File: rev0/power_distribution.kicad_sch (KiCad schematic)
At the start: 84 parts, among them Q1 PMOS, Q10 2PNP, Q11 2NPN, Q12 PMOS, Q13 2PNP, Q14 2PNP, Q15 2PNP, Q2 PMOS, Q3 2NPN, Q4 PMOS, Q5 PMOS, Q6 PMOS, Q7 PMOS, Q8 2NPN, Q9 PMOS, U1 PAC1954

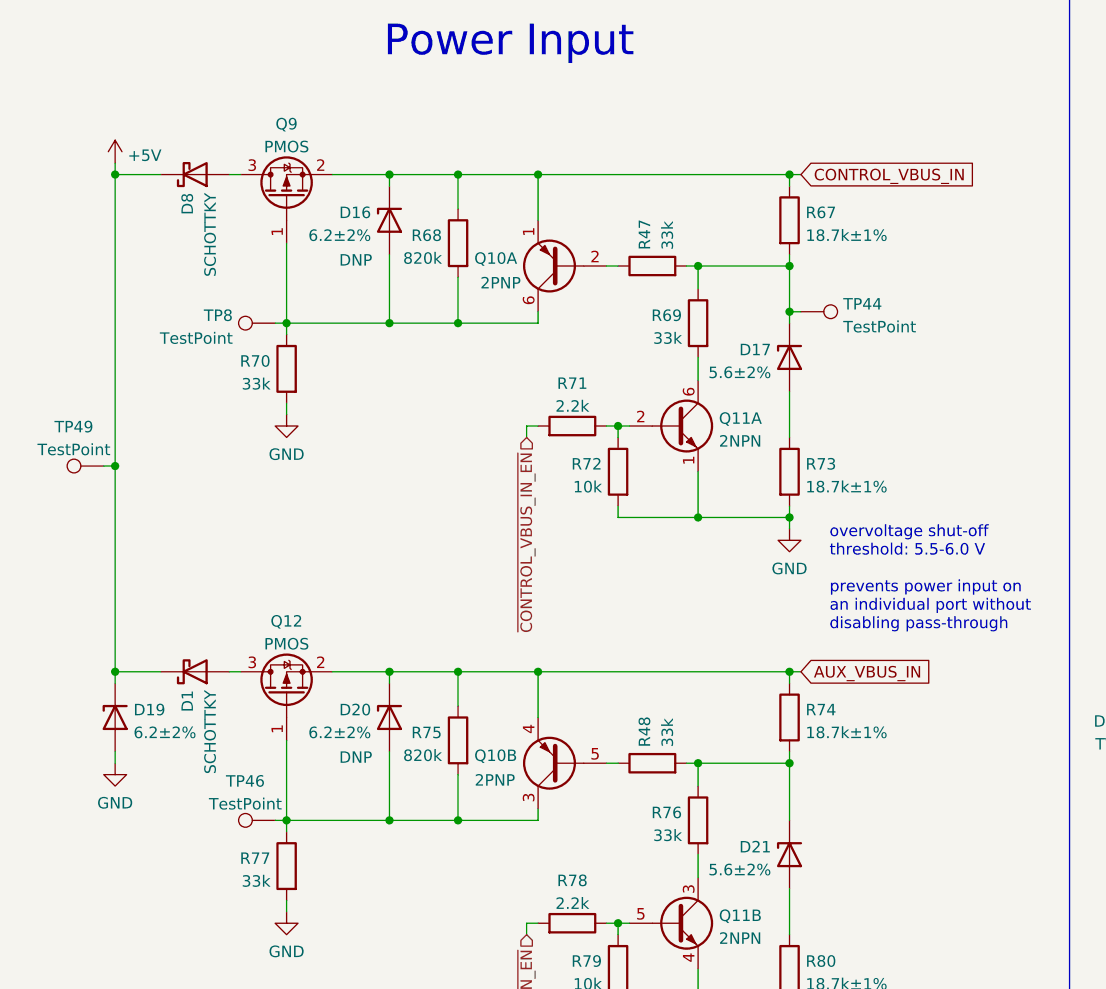
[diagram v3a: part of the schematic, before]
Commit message: hardware: update +5V input diodes
improve power dissipation
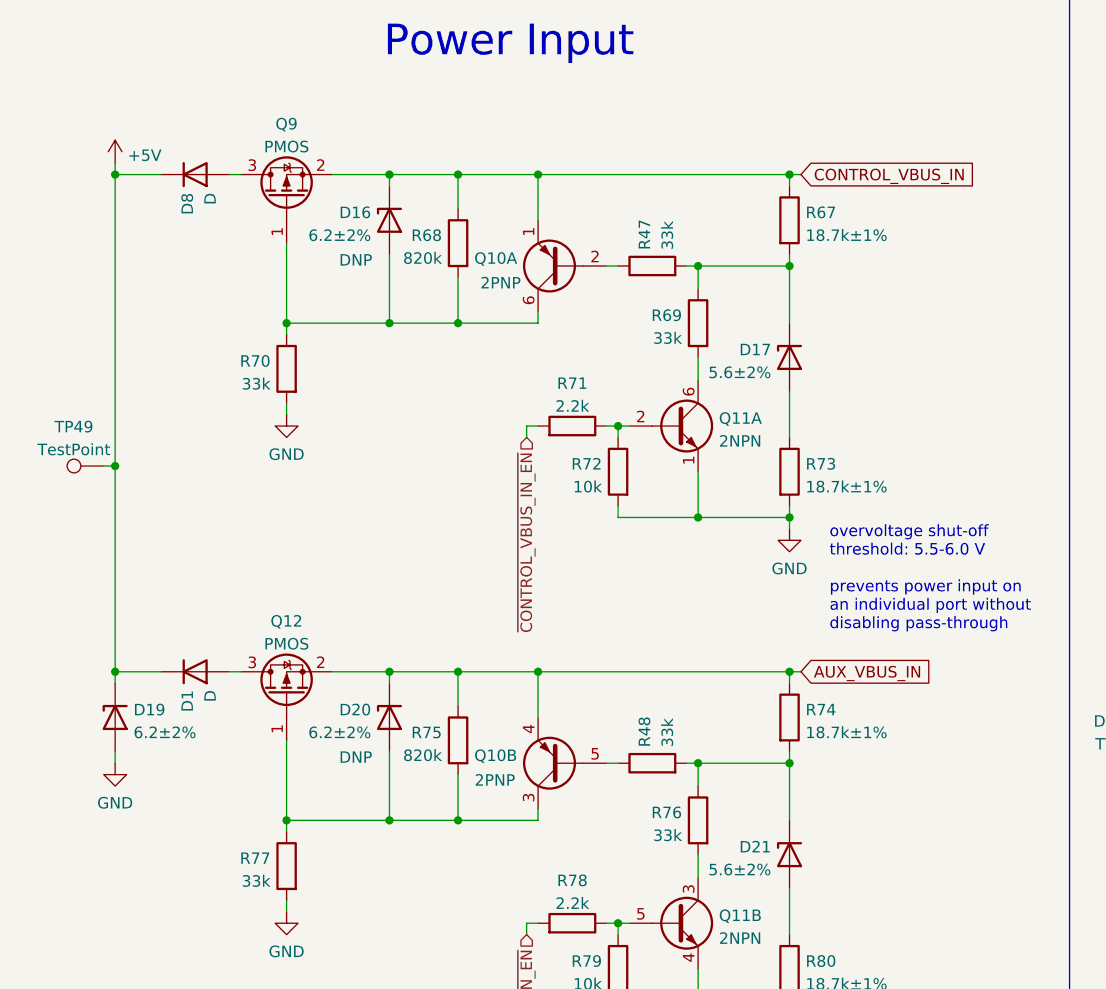
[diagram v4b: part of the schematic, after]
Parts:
- removed TP44, TP46, TP8: TestPoint, TestPoint:TestPoint_Pad_D1.0mm, symbol Connector:TestPoint
- D1, D8: value SCHOTTKY -> D; footprint Diode_SMD:D_SOD-123F -> luna:D_SOD-123FL; symbol Device:D_Schottky -> Device:D; Manufacturer Nexperia -> Yangzhou Yangjie; Part Number PMEG10010ELRX -> U1D
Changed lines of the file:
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@@
   (junction (at 261.62 93.98) (diameter 0) (color 0 0 0 0)
   )
-  (junction (at 98.425 52.705) (diameter 0) (color 0 0 0 0)
-  )
   (junction (at 139.065 45.085) (diameter 0) (color 0 0 0 0)
   )
@@
     (stroke (width 0) (type default) (color 0 0 0 0))
   )
-  (wire (pts (xy 98.425 52.705) (xy 98.425 47.625))
+  (wire (pts (xy 98.425 47.625) (xy 98.425 53.975))
     (stroke (width 0) (type default) (color 0 0 0 0))
   )
@@
     (stroke (width 0) (type default) (color 0 0 0 0))
   )
-  (wire (pts (xy 41.275 109.22) (xy 42.545 109.22))
-    (stroke (width 0) (type default) (color 0 0 0 0))
-  )
   (wire (pts (xy 62.23 179.07) (xy 60.96 179.07))
     (stroke (width 0) (type default) (color 0 0 0 0))
@@
     (stroke (width 0) (type default) (color 0 0 0 0))
   )
-  (wire (pts (xy 99.695 52.705) (xy 98.425 52.705))
-    (stroke (width 0) (type default) (color 0 0 0 0))
-  )
   (wire (pts (xy 179.07 129.54) (xy 187.96 129.54))
     (stroke (width 0) (type default) (color 0 0 0 0))
@@
     (stroke (width 0) (type default) (color 0 0 0 0))
   )
-  (wire (pts (xy 41.275 53.975) (xy 42.545 53.975))
-    (stroke (width 0) (type default) (color 0 0 0 0))
-  )
   (wire (pts (xy 139.065 46.355) (xy 139.065 45.085))
     (stroke (width 0) (type default) (color 0 0 0 0))
@@
     (stroke (width 0) (type default) (color 0 0 0 0))
   )
-  (wire (pts (xy 98.425 53.975) (xy 98.425 52.705))
-    (stroke (width 0) (type default) (color 0 0 0 0))
-  )
   (wire (pts (xy 62.23 176.53) (xy 60.96 176.53))
     (stroke (width 0) (type default) (color 0 0 0 0))
@@
     (pin "2")
   )
-  (symbol (lib_id "Device:D_Schottky") (at 32.385 92.71 0) (mirror x) (unit 1)
+  (symbol (lib_id "Device:D") (at 32.385 92.71 0) (mirror x) (unit 1)
     (in_bom yes) (on_board yes)
     (property "Reference" "D1" (id 0) (at 31.5503 94.742 90)
       (effects (font (size 1.27 1.27)) (justify left))
     )
-    (property "Value" "SCHOTTKY" (id 1) (at 34.0872 94.742 90)
+    (property "Value" "D" (id 1) (at 34.0872 94.742 90)
       (effects (font (size 1.27 1.27)) (justify left))
     )
-    (property "Footprint" "Diode_SMD:D_SOD-123F" (id 2) (at 32.385 92.71 0)
+    (property "Footprint" "luna:D_SOD-123FL" (id 2) (at 32.385 92.71 0)
       (effects (font (size 1.27 1.27)) hide)
     )
-    (property "Datasheet" "https://assets.nexperia.com/documents/data-sheet/PMEG10010ELR.pdf" (id 3) (at 32.385 92.71 0)
+    (property "Datasheet" "https://www.21yangjie.com/ggs/zlqj/ckfhejg/U1A%20THRU%20U1J.pdf" (id 3) (at 32.385 92.71 0)
       (effects (font (size 1.27 1.27)) hide)
     )
-    (property "Manufacturer" "Nexperia" (id 5) (at 32.385 92.71 0)
+    (property "Manufacturer" "Yangzhou Yangjie" (id 5) (at 32.385 92.71 0)
       (effects (font (size 1.27 1.27)) hide)
     )
-    (property "Part Number" "PMEG10010ELRX" (id 6) (at 32.385 92.71 0)
+    (property "Part Number" "U1D" (id 6) (at 32.385 92.71 0)
       (effects (font (size 1.27 1.27)) hide)
     )
-    (property "Description" "DIODE SCHOTTKY 100V 1A SOD123W" (id 7) (at 32.385 92.71 0)
+    (property "Description" "SOD-123FL 200V 1.0A  Diodes Rec" (id 7) (at 32.385 92.71 0)
       (effects (font (size 1.27 1.27)) hide)
     )
@@
     (pin "2")
   )
-  (symbol (lib_id "Connector:TestPoint") (at 41.275 109.22 90) (unit 1)
-    (in_bom no) (on_board yes) (fields_autoplaced)
-    (property "Reference" "TP46" (id 0) (at 37.973 104.8852 90))
-    (property "Value" "TestPoint" (id 1) (at 37.973 107.4221 90))
-    (property "Footprint" "TestPoint:TestPoint_Pad_D1.0mm" (id 2) (at 41.275 104.14 0)
-      (effects (font (size 1.27 1.27)) hide)
-    )
-    (property "Datasheet" "~" (id 3) (at 41.275 104.14 0)
-      (effects (font (size 1.27 1.27)) hide)
-    )
-    (pin "1")
-  )
   (symbol (lib_id "Device:Q_Dual_PNP_PNP_E1B1C2E2B2C1") (at 181.61 100.33 180) (unit 2)
     (in_bom yes) (on_board yes)
@@
     (pin "1")
   )
-  (symbol (lib_id "Connector:TestPoint") (at 99.695 52.705 270) (mirror x) (unit 1)
-    (in_bom no) (on_board yes) (fields_autoplaced)
-    (property "Reference" "TP44" (id 0) (at 104.394 51.8703 90)
-      (effects (font (size 1.27 1.27)) (justify left))
-    )
-    (property "Value" "TestPoint" (id 1) (at 104.394 54.4072 90)
-      (effects (font (size 1.27 1.27)) (justify left))
-    )
-    (property "Footprint" "TestPoint:TestPoint_Pad_D1.0mm" (id 2) (at 99.695 47.625 0)
-      (effects (font (size 1.27 1.27)) hide)
-    )
-    (property "Datasheet" "~" (id 3) (at 99.695 47.625 0)
-      (effects (font (size 1.27 1.27)) hide)
-    )
-    (pin "1")
-  )
   (symbol (lib_id "Device:D_Zener") (at 275.59 99.06 90) (mirror x) (unit 1)
     (in_bom yes) (on_board yes) (fields_autoplaced)
@@
     (pin "2")
   )
-  (symbol (lib_id "Connector:TestPoint") (at 41.275 53.975 90) (unit 1)
-    (in_bom no) (on_board yes) (fields_autoplaced)
-    (property "Reference" "TP8" (id 0) (at 36.576 53.1403 90)
-      (effects (font (size 1.27 1.27)) (justify left))
-    )
-    (property "Value" "TestPoint" (id 1) (at 36.576 55.6772 90)
-      (effects (font (size 1.27 1.27)) (justify left))
-    )
-    (property "Footprint" "TestPoint:TestPoint_Pad_D1.0mm" (id 2) (at 41.275 48.895 0)
-      (effects (font (size 1.27 1.27)) hide)
-    )
-    (property "Datasheet" "~" (id 3) (at 41.275 48.895 0)
-      (effects (font (size 1.27 1.27)) hide)
-    )
-    (pin "1")
-  )
   (symbol (lib_id "Device:D_Zener") (at 23.495 97.79 90) (mirror x) (unit 1)
     (in_bom yes) (on_board yes) (fields_autoplaced)
@@
     (pin "4")
   )
-  (symbol (lib_id "Device:D_Schottky") (at 32.385 37.465 0) (mirror x) (unit 1)
+  (symbol (lib_id "Device:D") (at 32.385 37.465 0) (mirror x) (unit 1)
     (in_bom yes) (on_board yes)
     (property "Reference" "D8" (id 0) (at 31.5503 39.497 90)
       (effects (font (size 1.27 1.27)) (justify left))
     )
-    (property "Value" "SCHOTTKY" (id 1) (at 34.0872 39.497 90)
+    (property "Value" "D" (id 1) (at 34.0872 39.497 90)
       (effects (font (size 1.27 1.27)) (justify left))
     )
-    (property "Footprint" "Diode_SMD:D_SOD-123F" (id 2) (at 32.385 37.465 0)
+    (property "Footprint" "luna:D_SOD-123FL" (id 2) (at 32.385 37.465 0)
       (effects (font (size 1.27 1.27)) hide)
     )
-    (property "Datasheet" "https://assets.nexperia.com/documents/data-sheet/PMEG10010ELR.pdf" (id 3) (at 32.385 37.465 0)
+    (property "Datasheet" "https://www.21yangjie.com/ggs/zlqj/ckfhejg/U1A%20THRU%20U1J.pdf" (id 3) (at 32.385 37.465 0)
       (effects (font (size 1.27 1.27)) hide)
     )
-    (property "Manufacturer" "Nexperia" (id 5) (at 32.385 37.465 0)
+    (property "Manufacturer" "Yangzhou Yangjie" (id 5) (at 32.385 37.465 0)
       (effects (font (size 1.27 1.27)) hide)
     )
-    (property "Part Number" "PMEG10010ELRX" (id 6) (at 32.385 37.465 0)
+    (property "Part Number" "U1D" (id 6) (at 32.385 37.465 0)
       (effects (font (size 1.27 1.27)) hide)
     )
-    (property "Description" "DIODE SCHOTTKY 100V 1A SOD123W" (id 7) (at 32.385 37.465 0)
+    (property "Description" "SOD-123FL 200V 1.0A  Diodes Rec" (id 7) (at 32.385 37.465 0)
       (effects (font (size 1.27 1.27)) hide)
     )

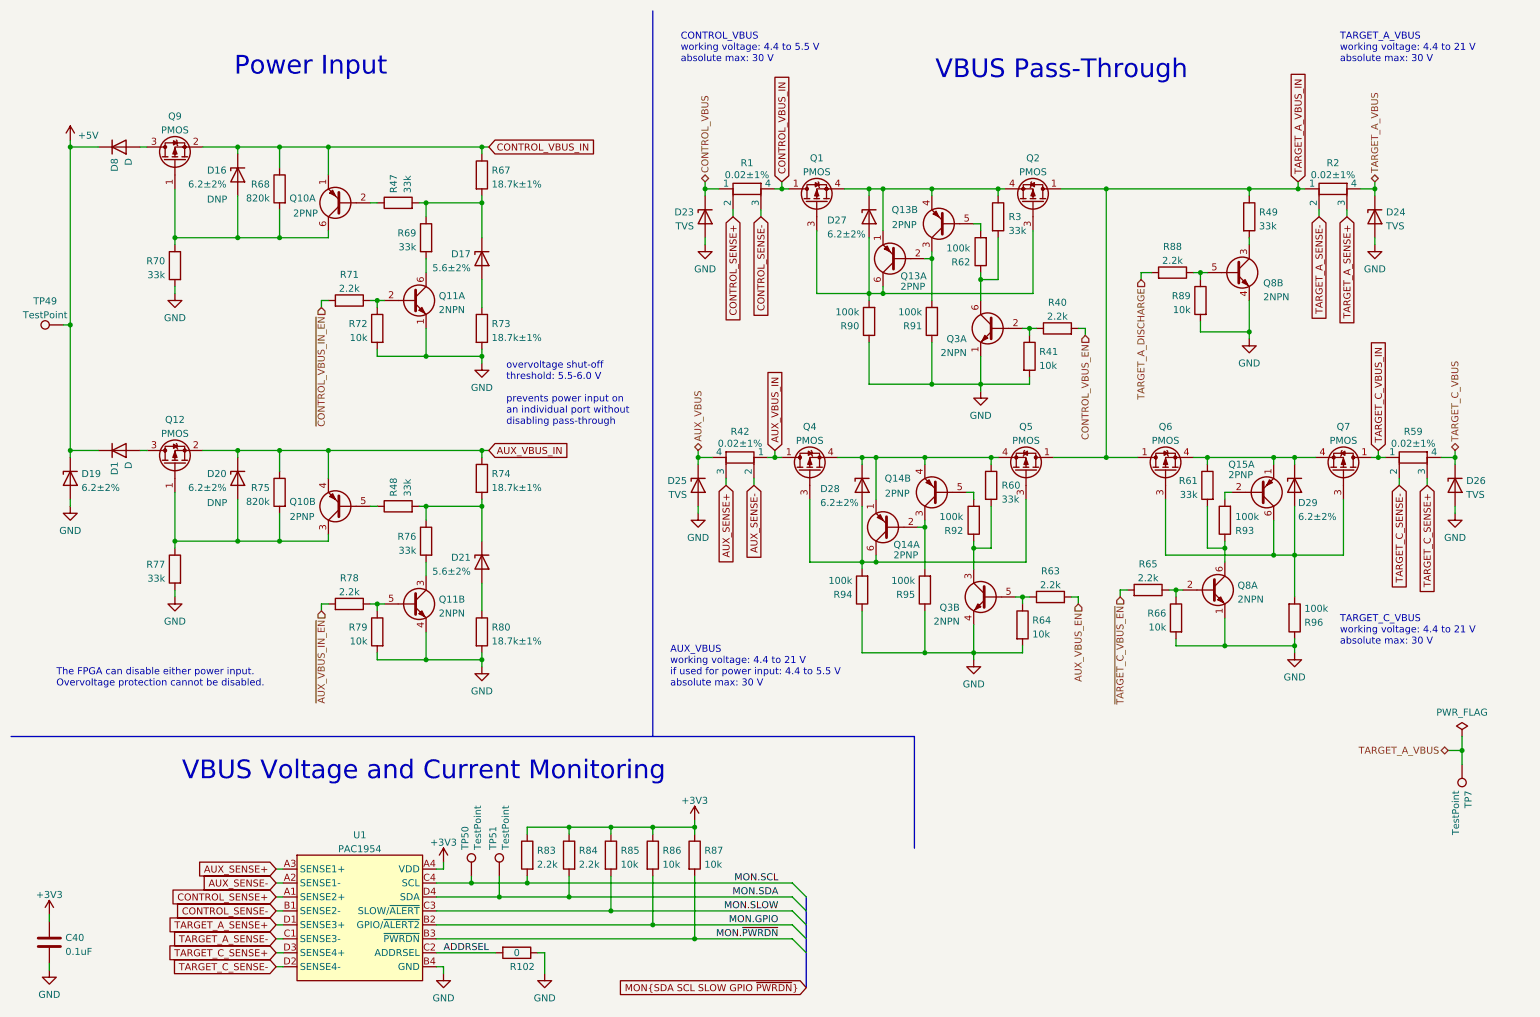
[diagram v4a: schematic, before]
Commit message: hardware: update current sense resistor footprint
- use standard 0603 footprint for reliable assembly
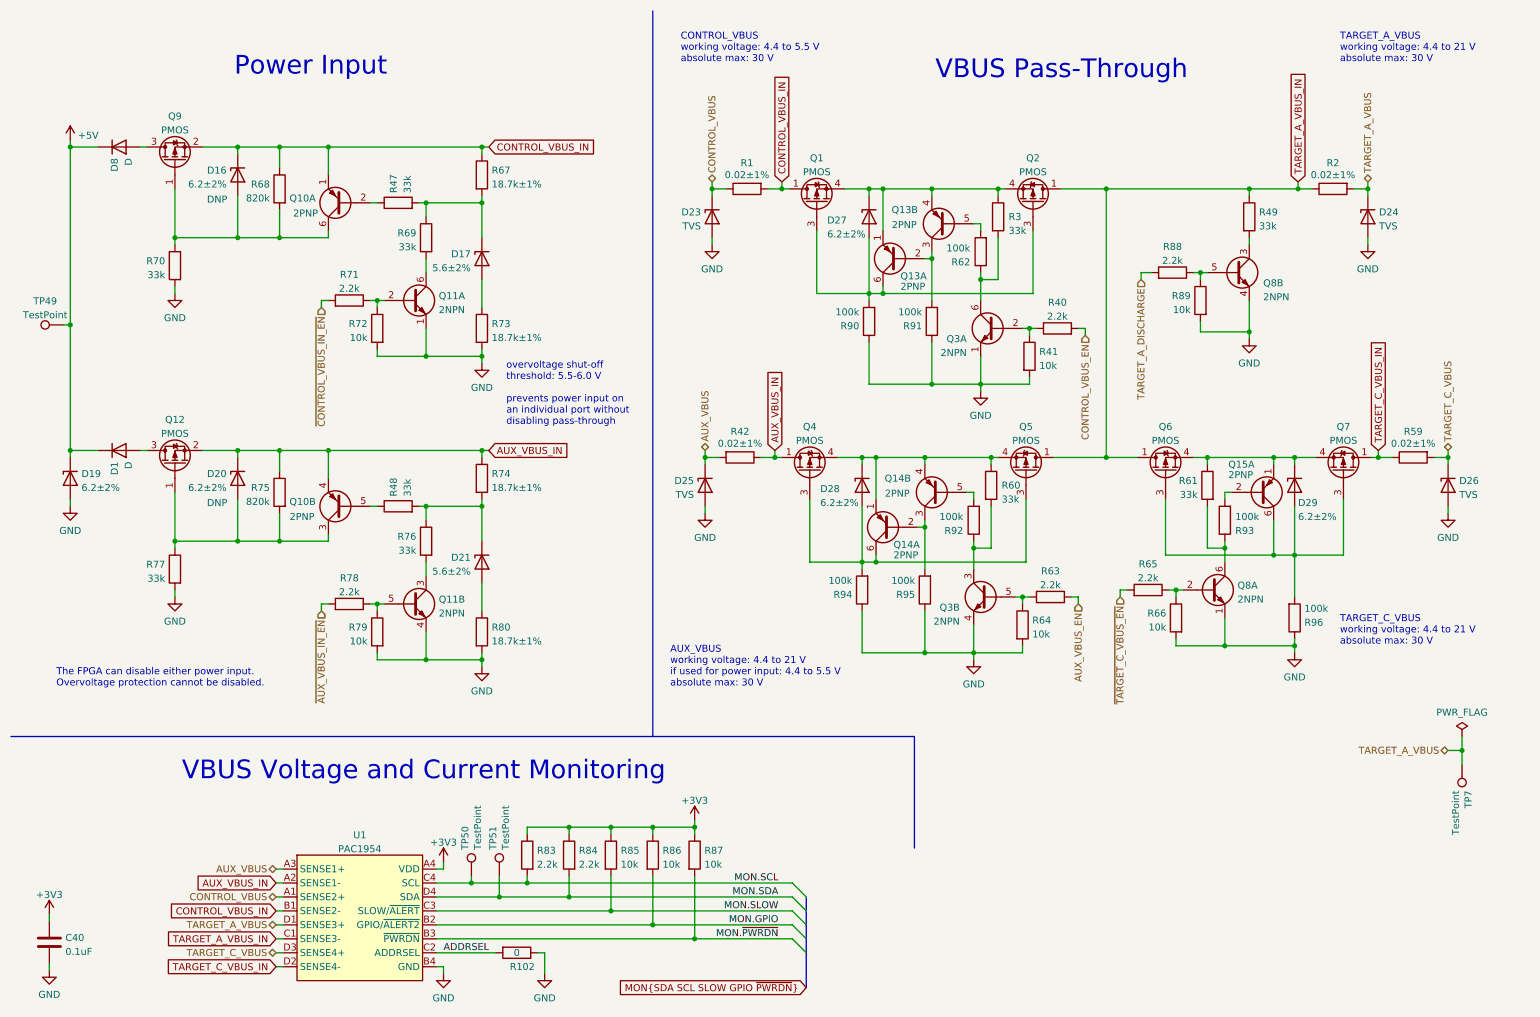
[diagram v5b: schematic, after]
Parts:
- R1, R2, R42, R59: footprint luna:R_0603_1608Metric_Current_Sense -> Resistor_SMD:R_0603_1608Metric; symbol Device:R_Shunt -> Device:R
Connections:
- net AUX_VBUS: now also R42.2, U1.A3 (SENSE1+); no longer R42.4
- net AUX_VBUS_IN: now also U1.A2 (SENSE1-)
- net CONTROL_VBUS: now also U1.A1 (SENSE2+)
- net CONTROL_VBUS_IN: now also R1.2, U1.B1 (SENSE2-); no longer R1.4
- net TARGET_A_VBUS: now also R2.2, U1.D1 (SENSE3+); no longer R2.4
- net TARGET_A_VBUS_IN: now also U1.C1 (SENSE3-)
- net TARGET_C_VBUS: now also R59.2, U1.D3 (SENSE4+); no longer R59.4
- net TARGET_C_VBUS_IN: now also U1.D2 (SENSE4-)
- removed net AUX_SENSE+: R42.3, U1.A3 (SENSE1+)
- removed net AUX_SENSE-: R42.2, U1.A2 (SENSE1-)
- removed net CONTROL_SENSE+: R1.2, U1.A1 (SENSE2+)
- removed net CONTROL_SENSE-: R1.3, U1.B1 (SENSE2-)
- removed net TARGET_A_SENSE+: R2.3, U1.D1 (SENSE3+)
- removed net TARGET_A_SENSE-: R2.2, U1.C1 (SENSE3-)
- removed net TARGET_C_SENSE+: R59.3, U1.D3 (SENSE4+)
- removed net TARGET_C_SENSE-: R59.2, U1.D2 (SENSE4-)
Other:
- moved on the sheet: D23, D24, D25, D26
